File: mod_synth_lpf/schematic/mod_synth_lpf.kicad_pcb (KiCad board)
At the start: 2 copper layers, 41.3 x 109.2 mm, 42 parts, among them J1 AudioJack2, J2 AudioJack2, J3 AudioJack2, J4 Conn_02x08_Odd_Even, J5 Conn_01x07_Female, J6 Conn_01x07_Male, J7 Conn_01x07_Female, J8 Conn_01x07_Male, Q1 BC558, Q2 BC558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

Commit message: Try to clean up layout
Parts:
- moved R8 55.4 mm to (106.2, 98.6), turned to 90 degrees
- moved R5 38.1 mm to (72.6, 64.5), turned to 270 degrees
- moved R9 34.8 mm to (110.2, 44.2)
- moved R2 27.9 mm to (88.9, 74.7)
- moved R1 23.9 mm to (109.7, 75.7), turned to 270 degrees
- moved U1 15.9 mm to (110.2, 70.6), turned to 90 degrees
- moved R11 14.7 mm to (95.5, 44.2)
- moved R3 14.6 mm to (99.1, 85.9)
- moved R17 12.7 mm to (102.6, 98.6)
- moved R6 12.4 mm to (102.6, 75.7), turned to 270 degrees
- moved R10 10.2 mm to (99.1, 88.4), turned to 270 degrees
- moved R13 10.2 mm to (109.7, 88.4), turned to 270 degrees
- moved C6 6.20 mm to (106.7, 126.5), turned to 270 degrees
- moved C2 5.59 mm to (106.7, 103.1), turned to 270 degrees
- moved C4 4.96 mm to (72.6, 80.8), turned to 270 degrees
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
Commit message: Layout first PCB
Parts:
- moved C7 24.8 mm to (83.2, 61.6), turned to 0 degrees
- moved C4 19.9 mm to (78.1, 61.6), turned to 180 degrees
- moved R11 14.7 mm to (110.2, 44.2)
- moved R9 14.7 mm to (95.5, 44.2)
- moved R2 14.2 mm to (88.3, 88.9)
- moved R5 14.2 mm to (72.6, 78.7)
- moved R16 10.2 mm to (95.5, 31.5), turned to 270 degrees
- moved R3 7.11 mm to (106.2, 85.9)
- moved R6 3.56 mm to (99.1, 75.7)
- moved R7 3.56 mm to (102.6, 85.9)
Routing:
- net /INDICATOR_1_PCB_B: track 0.00 -> 78.5 mm
- net /INDICATOR_2_PCB_B: track 0.00 -> 75.1 mm
- net /-12_PCB_B: track 0.00 -> 69.2 mm
- net /+12_PCB_B: track 0.00 -> 63.1 mm
- net /CUT_OFF_PCB_B: track 0.00 -> 62.5 mm
- net /AUDIO_OUT_PCB_B: track 0.00 -> 49.1 mm
- net /RESONANCE_PCB_B: track 0.00 -> 34.1 mm
- net Net-(J3-PadT): track 0.00 -> 31.8 mm
- net /SWB_PCB_B: track 0.00 -> 30.0 mm
- net Net-(C4-Pad2): track 0.00 -> 25.8 mm
- net Net-(C7-Pad2): track 0.00 -> 21.0 mm
- net Net-(J1-PadT): track 0.00 -> 19.5 mm
- net Net-(R5-Pad2): track 0.00 -> 12.3 mm
- net /SWA_PCB_B: track 0.00 -> 8.92 mm
- net /CV_PCB_B: track 0.00 -> 8.91 mm
- added copper zone on B.Cu, net /GND_PCB_B
- added copper zone on F.Cu, net /GND_PCB_B

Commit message: Layout 6hp board
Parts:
- moved J5 65.9 mm to (66.0, 77.5), turned to 0 degrees
- moved J6 64.3 mm to (98.4, 77.5), turned to 180 degrees
- moved R3 60.9 mm to (66.0, 40.0)
- moved R17 57.5 mm to (87.0, 43.2), turned to 270 degrees
- moved J8 54.2 mm to (123.2, 77.5), turned to 180 degrees
- moved C2 53.8 mm to (71.8, 62.2)
- moved Q2 50.5 mm to (67.3, 60.3), turned to 270 degrees
- moved C3 48.7 mm to (70.5, 74.9)
- moved Q1 48.0 mm to (66.7, 69.2), turned to 90 degrees
- moved C1 46.6 mm to (87.0, 74.9)
- moved R5 43.3 mm to (115.6, 73.0), turned to 180 degrees
- moved R4 41.4 mm to (69.8, 53.3)
- moved R12 41.3 mm to (67.3, 99.7), turned to 0 degrees
- moved D2 40.7 mm to (114.9, 109.9)
- moved C7 39.4 mm to (122.6, 59.7), turned to 270 degrees
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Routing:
- net -12V: track 0.00 -> 127.2 mm
- net +12V: track 0.00 -> 105.8 mm, vias 0 -> 1
- net /SWB_PCB_A: track 0.00 -> 76.1 mm
- net GND: track 0.00 -> 64.0 mm
- net /INDICATOR_1_PCB_A: track 0.00 -> 62.8 mm, vias 0 -> 1
- net Net-(Q2-Pad2): track 0.00 -> 56.6 mm
- net Net-(Q1-Pad1): track 0.00 -> 56.6 mm
- net /CV_PCB_B: track 8.91 -> 63.4 mm
- net /INDICATOR_2_PCB_A: track 0.00 -> 50.6 mm
- net /SWA_PCB_A: track 0.00 -> 45.4 mm
- net /SWA_PCB_B: track 8.92 -> 48.2 mm
- net Net-(Q1-Pad3): track 0.00 -> 39.2 mm
- net /INDICATOR_1_PCB_B: track 78.5 -> 39.6 mm
- net Net-(C2-Pad2): track 0.00 -> 38.6 mm
- net Net-(C1-Pad1): track 0.00 -> 38.1 mm
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- added copper zone on B.Cu, net GND
- added copper zone on F.Cu, net GND
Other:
- board size 41.3 x 109.2 mm -> 62.2 x 109.2 mm

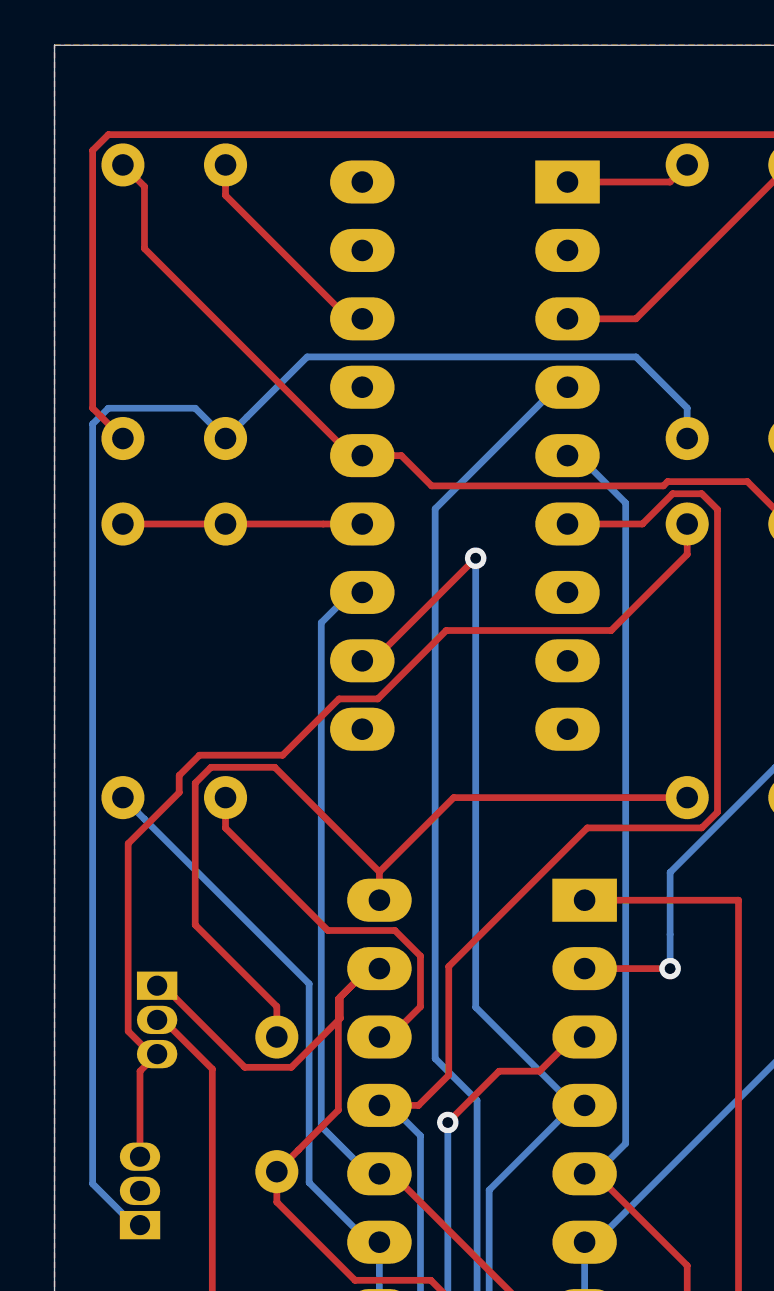
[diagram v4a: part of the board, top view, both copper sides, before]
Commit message: Update PCB to use 16 pin socket
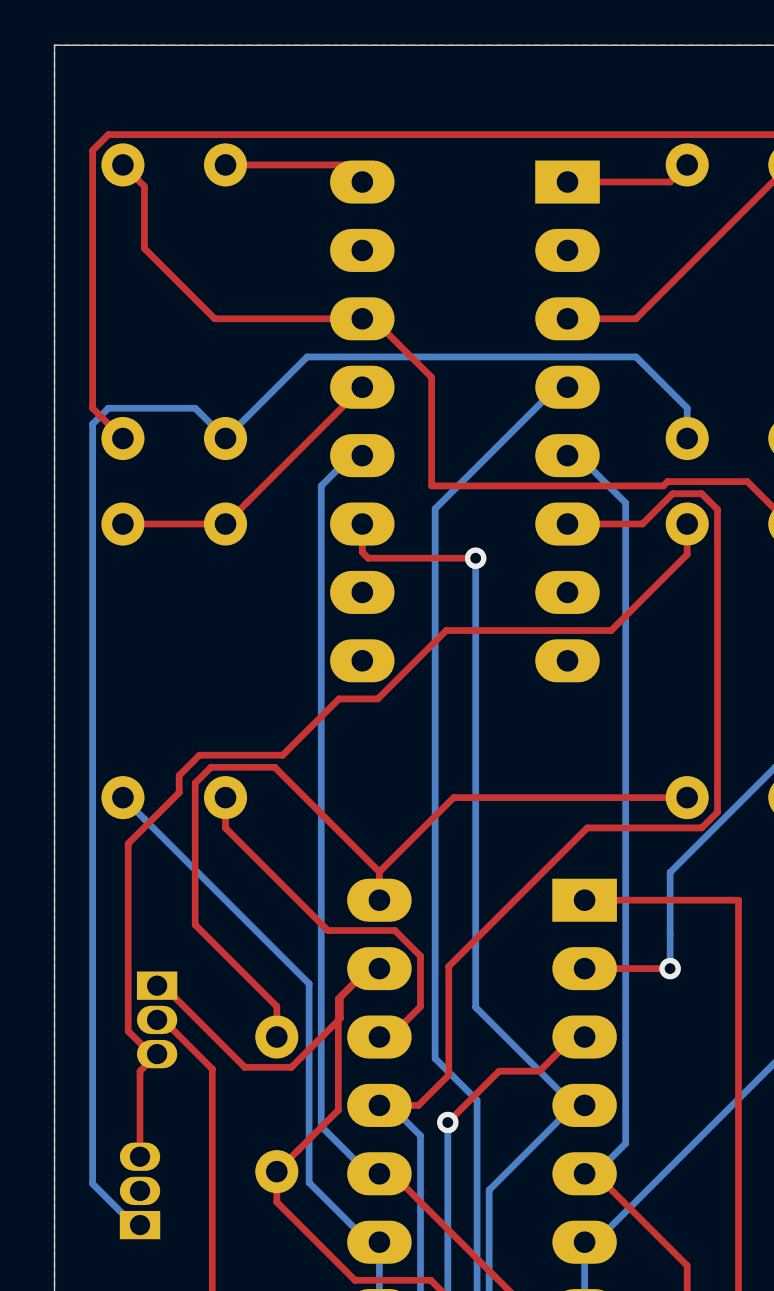
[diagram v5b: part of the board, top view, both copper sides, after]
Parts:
- U2: footprint Package_DIP:DIP-18_W7.62mm_Socket_LongPads -> Package_DIP:DIP-16_W7.62mm_Socket_LongPads
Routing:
- net /SWA_PCB_A: track 45.4 -> 50.5 mm
- net Net-(R3-Pad2): track 31.8 -> 34.6 mm
- net Net-(R16-Pad2): track 8.11 -> 5.34 mm
- net Net-(R4-Pad2): track 8.89 -> 11.0 mm
